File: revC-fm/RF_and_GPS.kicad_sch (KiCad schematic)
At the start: 44 parts, among them J2 SMPM-PS-P-HG-ST-TH-1, J3 SMPM-PS-P-HG-ST-TH-1, J4 SMPM-PS-P-HG-ST-TH-1, Q5 BSZ180P03NS3GATMA1, U20 RFM98PW, U21 RFM9xBreakout, U22 ORION B16, U23 RFM98PW, U24 RFM9xBreakout

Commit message: working revC
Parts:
- removed Q5 (x3): BSZ180P03NS3GATMA1, SierraLobo:PG-TSDSON-8_3.3x3.3mm, symbol SierraLobo:BSZ086
- removed R23 (x3): 1k, Resistor_SMD:R_0603_1608Metric, symbol Device:R_US
- C75: renamed from C91; Mfr. Part No (none) -> CGA4J1X7S1E106K125AE
- C76: renamed from C92; Mfr. Part No (none) -> CGA4J1X7S1E106K125AE
- Q42: value ~ -> NPN?
- Q5: Mfr. Part No (none) -> BSZ180P03NS3GATMA1
- R107: renamed from R173; footprint Resistor_SMD:R_0603_1608Metric -> Resistor_SMD:R_0402_1005Metric
- R108: renamed from R174; footprint Resistor_SMD:R_0603_1608Metric -> Resistor_SMD:R_0402_1005Metric
- R109: renamed from R177; footprint Resistor_SMD:R_0603_1608Metric -> Resistor_SMD:R_0402_1005Metric
- R110: renamed from R178; footprint Resistor_SMD:R_0603_1608Metric -> Resistor_SMD:R_0402_1005Metric
- R113: renamed from R181; footprint Resistor_SMD:R_0603_1608Metric -> Resistor_SMD:R_0402_1005Metric
- R114: renamed from R182; footprint Resistor_SMD:R_0603_1608Metric -> Resistor_SMD:R_0402_1005Metric
- R115: renamed from R183; footprint Resistor_SMD:R_0603_1608Metric -> Resistor_SMD:R_0402_1005Metric
- R116: renamed from R184; footprint Resistor_SMD:R_0603_1608Metric -> Resistor_SMD:R_0402_1005Metric
- R117: renamed from R185; footprint Resistor_SMD:R_0603_1608Metric -> Resistor_SMD:R_0402_1005Metric
- R118: renamed from R186; footprint Resistor_SMD:R_0603_1608Metric -> Resistor_SMD:R_0402_1005Metric
- R119: renamed from R187; footprint Resistor_SMD:R_0603_1608Metric -> Resistor_SMD:R_0402_1005Metric
- R120: renamed from R188; footprint Resistor_SMD:R_0603_1608Metric -> Resistor_SMD:R_0402_1005Metric
- R121: renamed from R189; footprint Resistor_SMD:R_0603_1608Metric -> Resistor_SMD:R_0402_1005Metric
- R195: value 100k -> 1Meg; footprint Resistor_SMD:R_0603_1608Metric -> Resistor_SMD:R_0402_1005Metric
- R196, R23: footprint Resistor_SMD:R_0603_1608Metric -> Resistor_SMD:R_0402_1005Metric
- U19: renamed from U20; Mfr. Part No (none) -> RFM98PW
- U21: renamed from U22; Mfr. Part No (none) -> ORION B16
- U22: renamed from U23; Mfr. Part No (none) -> RFM98PW
- renumbered U21 to U20, U24 to U23
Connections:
- net 3.3V: no longer Q5.1 (S), Q5.1 (S), R195.1, R195.1
- new net +5V: Q5.1 (S), Q5.1 (S), R195.1, R195.1

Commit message: working
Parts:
- renumbered C75 to C55, C76 to C56, R195 to R68, R107 to R77, R108 to R78, R109 to R79, R110 to R80, R113 to R83, R114 to R84, R115 to R85, R116 to R86, R117 to R87, R118 to R88, R119 to R89, R120 to R90, R121 to R91, U19 to U15, U20 to U16, U21 to U17, U22 to U18, U23 to U19

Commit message: almost done!!!!!
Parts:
- Q42: value NPN? -> MMBT3904T
- Q5: value BSZ180P03NS3GATMA1 -> BSZ180
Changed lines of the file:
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@@
       (effects (font (size 1.27 1.27)) (justify left))
     )
-    (property "Value" "NPN?" (at 153.4414 65.913 0)
+    (property "Value" "MMBT3904T" (at 153.4414 65.913 0)
       (effects (font (size 1.27 1.27)) (justify left))
     )
@@
       (effects (font (size 1.27 1.27)) (justify left))
     )
-    (property "Value" "NPN?" (at 140.7414 171.323 0)
+    (property "Value" "MMBT3904T" (at 140.7414 171.323 0)
       (effects (font (size 1.27 1.27)) (justify left))
     )
@@
       (effects (font (size 1.27 1.27)) (justify left))
     )
-    (property "Value" "NPN?" (at 233.68 66.675 0)
+    (property "Value" "MMBT3904T" (at 233.68 66.675 0)
       (effects (font (size 1.27 1.27)) (justify left))
     )
@@
       (effects (font (size 1.27 1.27)))
     )
-    (property "Value" "BSZ180P03NS3GATMA1" (at 169.926 152.908 0)
+    (property "Value" "BSZ180" (at 169.926 152.908 0)
       (effects (font (size 1.27 1.27)))
     )
@@
       (effects (font (size 1.27 1.27)))
     )
-    (property "Value" "BSZ180P03NS3GATMA1" (at 182.626 46.228 0)
+    (property "Value" "BSZ180" (at 182.626 46.228 0)
       (effects (font (size 1.27 1.27)))
     )
@@
       (effects (font (size 1.27 1.27)) (justify left))
     )
-    (property "Value" "BSZ180P03NS3GATMA1" (at 252.73 50.165 0)
-      (effects (font (size 1.27 1.27)) (justify left))
-    )
+    (property "Value" "BSZ180" (at 252.73 50.165 0)
+      (effects (font (size 1.27 1.27)) (justify left))
+    )

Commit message: updated fab files
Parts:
- C103: renamed from C55; Manufacturer (none) -> TDK
- C104: renamed from C56; Manufacturer (none) -> TDK
- J2, J3, J4: Manufacturer (none) -> Samtec
- Q42: footprint Package_TO_SOT_SMD:SOT-323_SC-70 -> Package_TO_SOT_SMD:SOT-523; Manufacturer (none) -> Diodes Incorporated; Mfr. Part No (none) -> MMBT3904T-7-F
- Q5: Manufacturer (none) -> Infineon
- R196: Manufacturer (none) -> Stackpole Electronics; Mfr. Part No (none) -> RMCF0402FT100K
- R220: renamed from R77; Manufacturer (none) -> Stackpole Electronics; Mfr. Part No (none) -> RMCF0402FT10K0
- R221: renamed from R78; Manufacturer (none) -> Panasonic; Mfr. Part No (none) -> ERJ-2GEJ102X
- R222: renamed from R79; Manufacturer (none) -> Panasonic; Mfr. Part No (none) -> ERJ-2GEJ102X
- R223: renamed from R80; Manufacturer (none) -> Panasonic; Mfr. Part No (none) -> ERJ-2GEJ102X
- R226: renamed from R83; Manufacturer (none) -> Panasonic; Mfr. Part No (none) -> ERJ-2GEJ102X
- R227: renamed from R84; Manufacturer (none) -> Panasonic; Mfr. Part No (none) -> ERJ-2GEJ102X
- R228: renamed from R85; Manufacturer (none) -> Panasonic; Mfr. Part No (none) -> ERJ-2GEJ102X
- R229: renamed from R86; Manufacturer (none) -> Panasonic; Mfr. Part No (none) -> ERJ-2GEJ102X
- R23: Manufacturer (none) -> Panasonic; Mfr. Part No (none) -> ERJ-2GEJ102X
- R230: renamed from R87; Manufacturer (none) -> Stackpole Electronics; Mfr. Part No (none) -> RMCF0402FT10K0
- R231: renamed from R88; Manufacturer (none) -> Panasonic; Mfr. Part No (none) -> ERJ-2GEJ102X
- R232: renamed from R89; Manufacturer (none) -> Panasonic; Mfr. Part No (none) -> ERJ-2GEJ102X
- R233: renamed from R90; Manufacturer (none) -> Panasonic; Mfr. Part No (none) -> ERJ-2GEJ102X
- R234: renamed from R91; Manufacturer (none) -> Panasonic; Mfr. Part No (none) -> ERJ-2GEJ102X
- R68: Manufacturer (none) -> Stackpole Electronics; Mfr. Part No (none) -> RMCF0402FT1M00
- U24: renamed from U15; Manufacturer (none) -> HopeRF
- U25: renamed from U16; Manufacturer (none) -> HopeRF; Mfr. Part No (none) -> RFM98
- U26: renamed from U17; value ORION B16 -> ORION B16-C; Manufacturer (none) -> SkyTraq; Mfr. Part No ORION B16 -> ORION B16-C
- U27: renamed from U18; Manufacturer (none) -> HopeRF
- U28: renamed from U19; Manufacturer (none) -> HopeRF; Mfr. Part No (none) -> RFM98

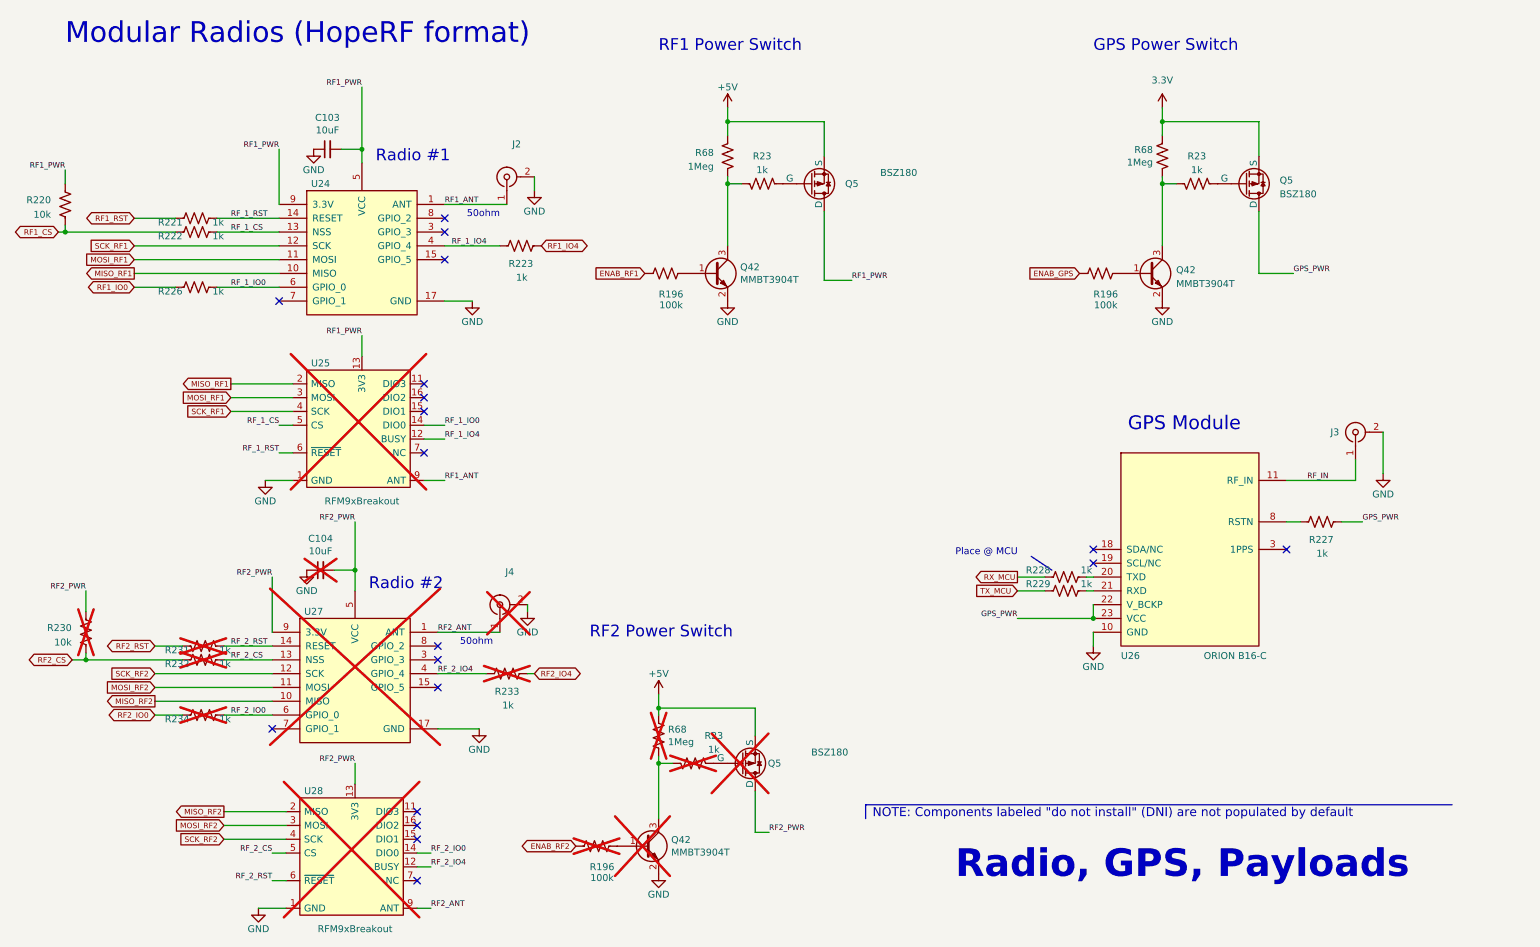
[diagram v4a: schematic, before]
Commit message: updated per review, improved docs
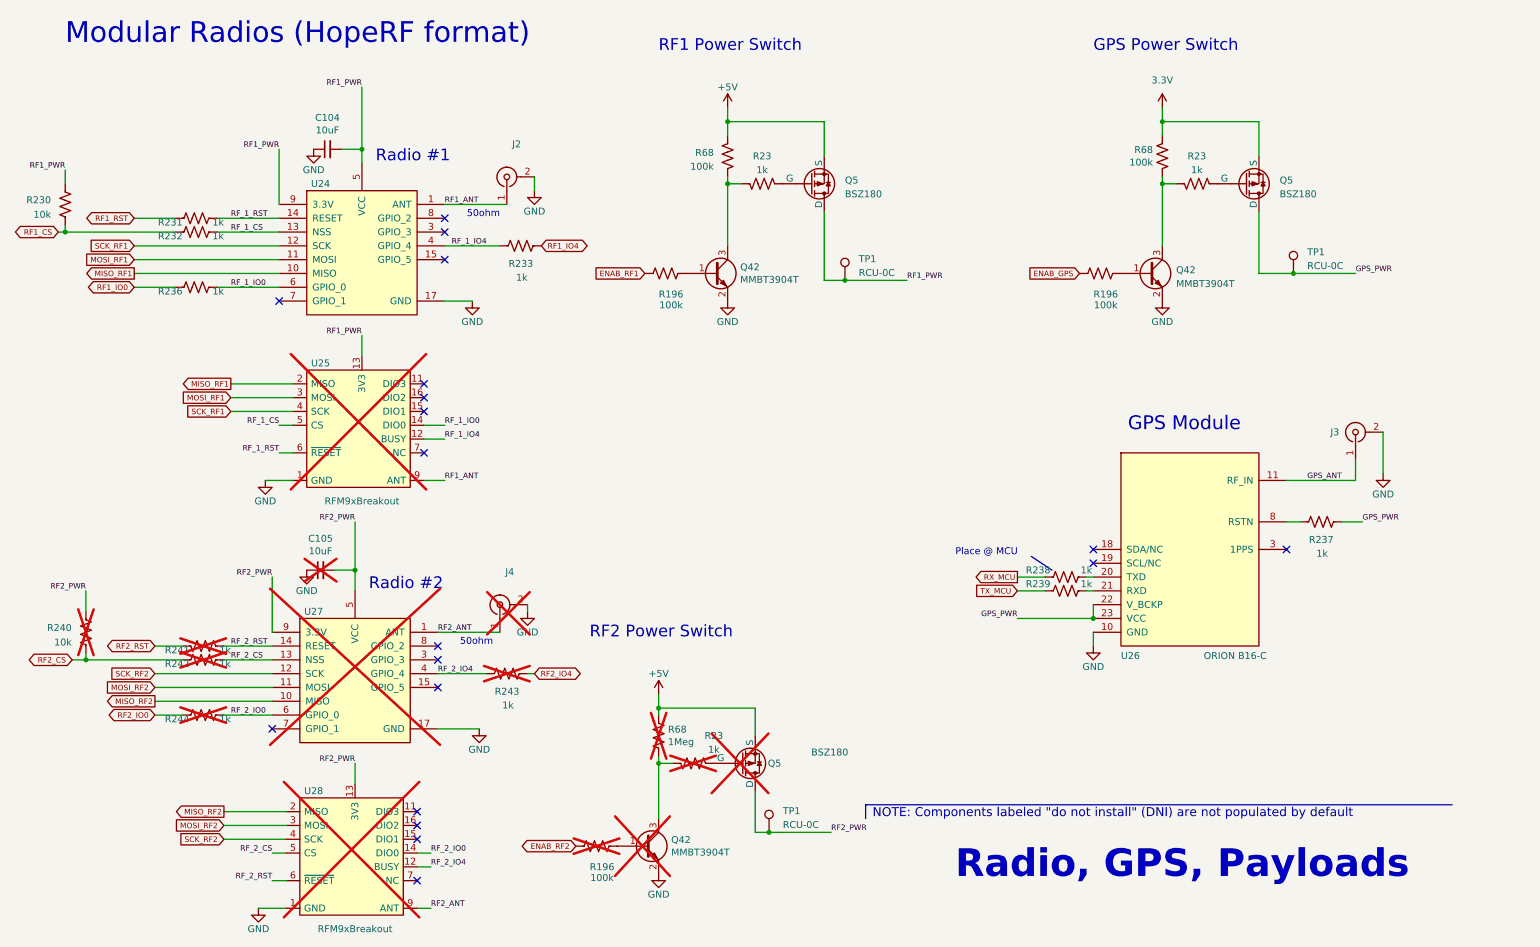
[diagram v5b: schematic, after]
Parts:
- added TP1 (x3): RCU-0C, SierraLobo:TestPoint_TE_RCU_0603, symbol Connector:TestPoint
- R68: value 1Meg -> 100k; Mfr. Part No RMCF0402FT1M00 -> RMCF0402FT100K
- renumbered C103 to C104, C104 to C105, R220 to R230, R221 to R231, R222 to R232, R223 to R233, R226 to R236, R227 to R237, R228 to R238, R229 to R239, R230 to R240, R231 to R241, R232 to R242, R233 to R243, R234 to R244
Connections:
- net GPS_PWR: now also TP1.1
- net RF1_PWR: now also TP1.1
- net RF2_PWR: now also TP1.1
- net RF_IN renamed GPS_ANT
